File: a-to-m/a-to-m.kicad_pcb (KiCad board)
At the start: 2 copper layers, 94 x 104.8 mm, 0 parts

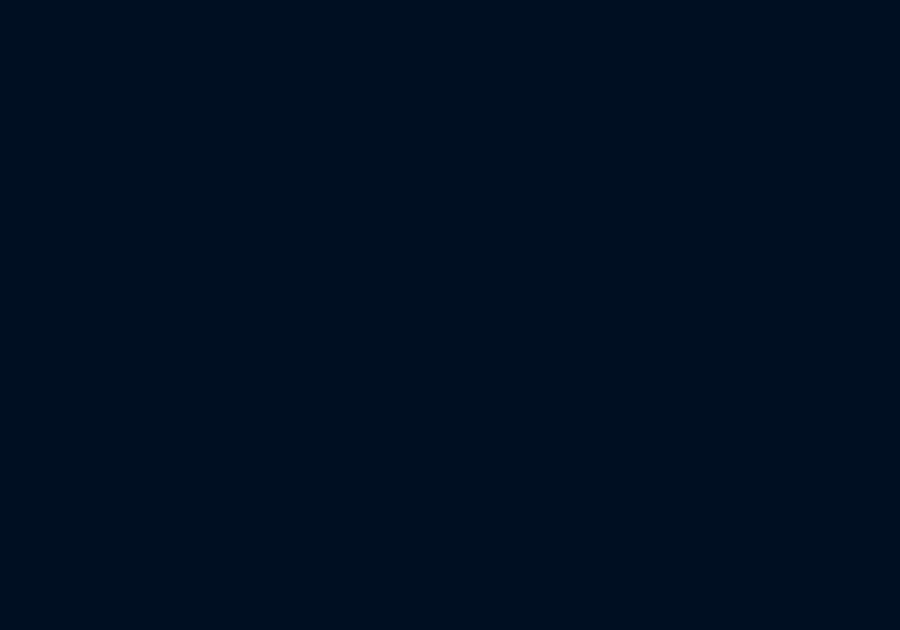
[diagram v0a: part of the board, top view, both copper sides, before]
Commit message: Add MCU
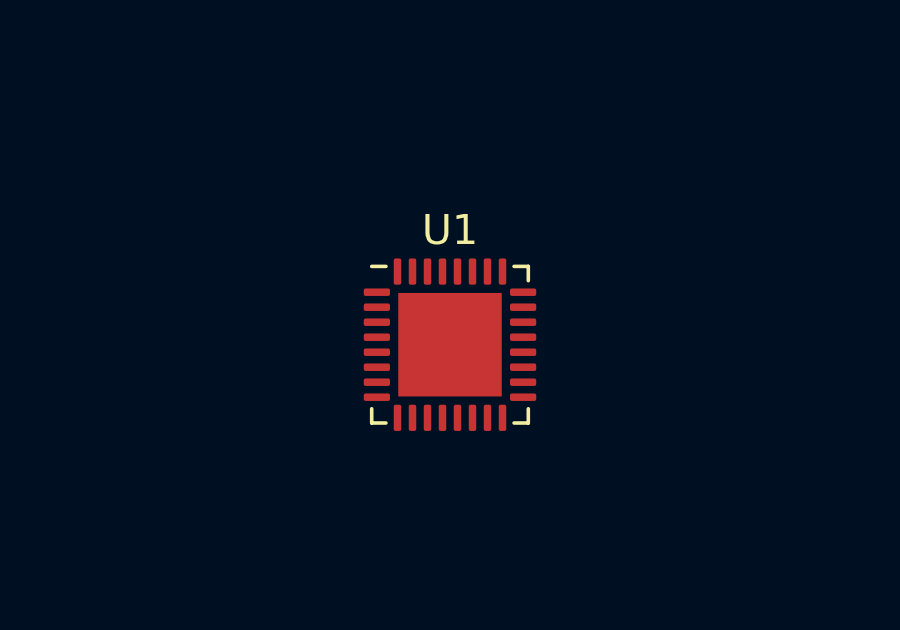
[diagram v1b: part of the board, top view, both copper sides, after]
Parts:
- added U1: ESP8285, Package_DFN_QFN:QFN-32-1EP_5x5mm_P0.5mm_EP3.45x3.45mm, F.Cu at (153.2, 101.9)

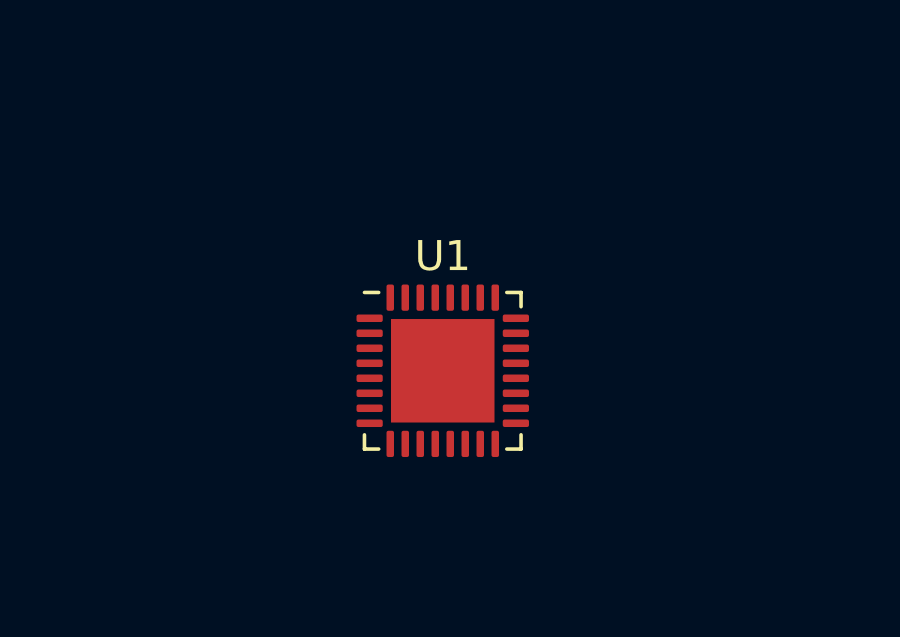
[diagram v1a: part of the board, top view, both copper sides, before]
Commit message: Use generic QFN32 package
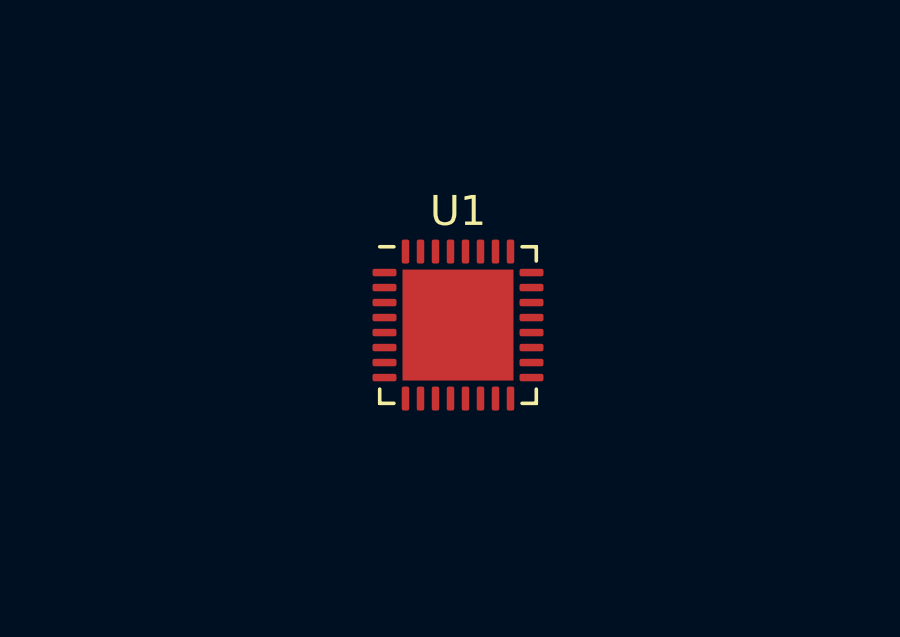
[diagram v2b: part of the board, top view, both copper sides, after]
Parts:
- U1: footprint Package_DFN_QFN:QFN-32-1EP_5x5mm_P0.5mm_EP3.45x3.45mm -> Package_DFN_QFN:QFN-32-1EP_5x5mm_P0.5mm_EP3.7x3.7mm
- moved U1 1.61 mm to (153.7, 100.3)
